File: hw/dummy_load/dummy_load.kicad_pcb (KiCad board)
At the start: 4 copper layers, 100 x 87 mm, 116 parts, among them J1 12V optional, J10 Calib gain, J11 Calib divider, J12 12V in, J2 NTC DUT, J3 NTC Ambient, J4 NTC Heatsink, J5 Fan1, J6 Fan2, J7 NTC Heatsink, J8 NTC Heatsink, J9 NTC Heatsink, Q1 DMN2056U, Q10 DMG2305UX-7, Q2 IRL540NPBF, Q3 IRL540NPBF, Q4 IRL540NPBF, Q5 IRL540NPBF, Q6 IRL540NPBF, Q7 IRL540NPBF, Q8 IRL540NPBF, Q9 IRL540NPBF, U1 LM358, U2 AD620, U21 LM4040B30FTA, U3 LM4040B30FTA, U4 PHOENIX_1017503, U5 74HC4051, U6 AD5272BCP, U7 AD5272BCP, U8 AMS1117-5.0

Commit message: Fix digipot cap value
Signed-off-by: Mateusz Pajak <22417805+Tai-Min@users.noreply.github.com>
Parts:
- C13, C14: value 100n -> 1u
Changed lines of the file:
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@@
 			)
 		)
-		(property "Value" "100n"
+		(property "Value" "1u"
 			(at 0 1.85 90)
 			(layer "F.Fab")
@@
 			)
 		)
-		(property "LCSC Part #" "C24497"
+		(property "LCSC Part #" "C1848"
 			(at 0 0 270)
 			(unlocked yes)
@@
 			)
 		)
-		(property "Value" "100n"
+		(property "Value" "1u"
 			(at 0 1.85 90)
 			(layer "F.Fab")
@@
 			)
 		)
-		(property "LCSC Part #" "C24497"
+		(property "LCSC Part #" "C1848"
 			(at 0 0 90)
 			(unlocked yes)

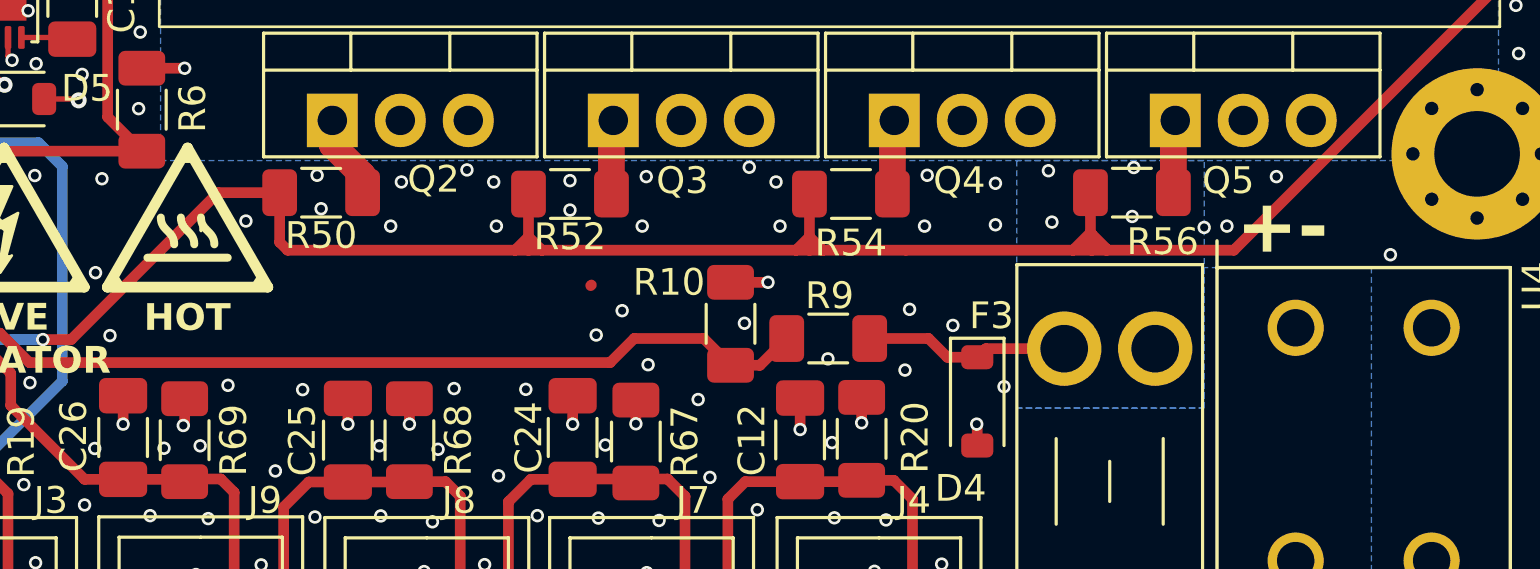
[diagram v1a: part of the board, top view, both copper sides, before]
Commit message: Fix hotspot, remove old schematic file
Signed-off-by: Mateusz Pajak <22417805+Tai-Min@users.noreply.github.com>
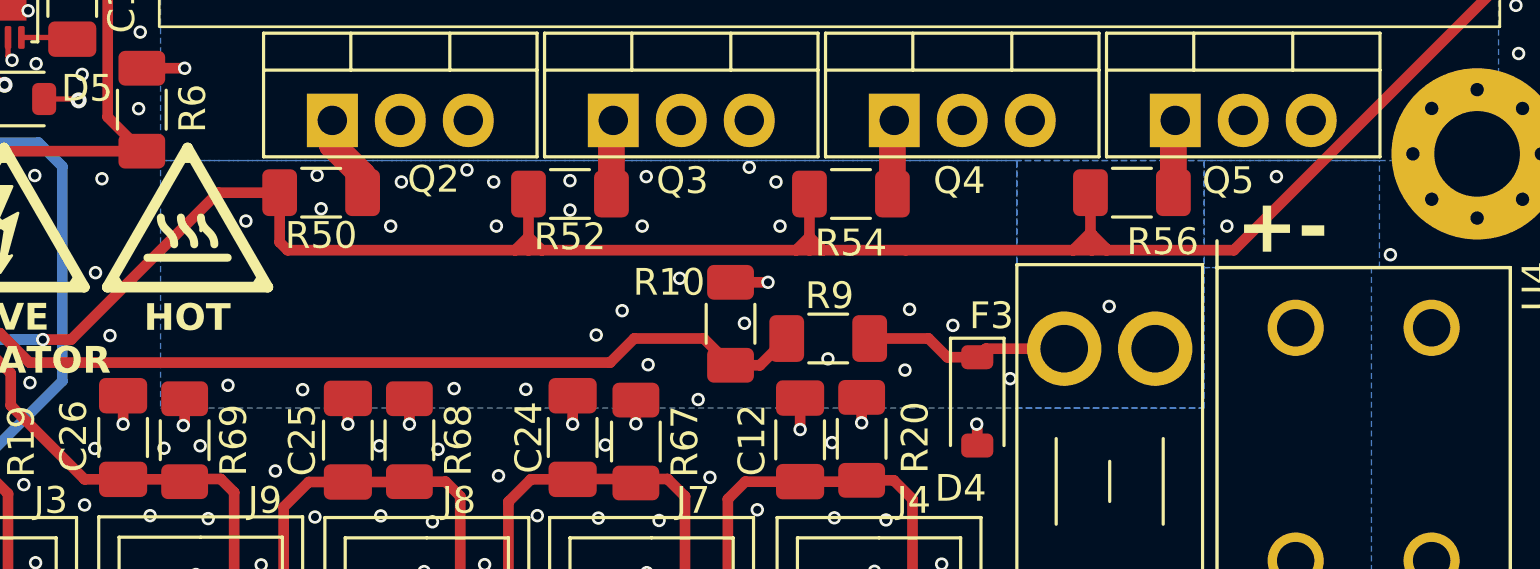
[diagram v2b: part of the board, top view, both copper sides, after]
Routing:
- net GND: vias 465 -> 458
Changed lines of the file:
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@@
 	)
 	(segment
-		(start 163.175 114.225)
-		(end 163.2 114.2)
-		(width 0.4)
-		(layer "F.Cu")
-		(net 4)
-	)
-	(segment
 		(start 123.69375 119.4)
 		(end 124.50625 119.4)
@@
 	)
 	(via
-		(at 180.41 111.85)
-		(size 0.5)
-		(drill 0.3)
-		(layers "F.Cu" "B.Cu")
-		(free yes)
-		(net 4)
-	)
-	(via
 		(at 146.44 99.95)
 		(size 0.5)
@@
 	)
 	(via
-		(at 175.75 110.1)
-		(size 0.5)
-		(drill 0.3)
-		(layers "F.Cu" "B.Cu")
-		(free yes)
-		(net 4)
-	)
-	(via
 		(at 134.91 89.63)
 		(size 0.5)
@@
 	)
 	(via
-		(at 175.65 112)
-		(size 0.5)
-		(drill 0.3)
-		(layers "F.Cu" "B.Cu")
-		(free yes)
-		(net 4)
-	)
-	(via
 		(at 134.75 127.21)
 		(size 0.5)
@@
 	)
 	(via
-		(at 180.28 109.93)
-		(size 0.5)
-		(drill 0.3)
-		(layers "F.Cu" "B.Cu")
-		(free yes)
-		(net 4)
-	)
-	(via
 		(at 133.43 53.81)
 		(size 0.5)
@@
 	)
 	(via
+		(at 182.55 115)
+		(size 0.5)
+		(drill 0.3)
+		(layers "F.Cu" "B.Cu")
+		(free yes)
+		(net 4)
+	)
+	(via
 		(at 150.29 111.81)
 		(size 0.5)
@@
 	)
 	(via
-		(at 186.1 112.05)
-		(size 0.5)
-		(drill 0.3)
-		(layers "F.Cu" "B.Cu")
-		(free yes)
-		(net 4)
-	)
-	(via
 		(at 109.56 61.34)
 		(size 0.5)
@@
 	)
 	(via
-		(at 183.47 109.81)
-		(size 0.5)
-		(drill 0.3)
-		(layers "F.Cu" "B.Cu")
-		(free yes)
-		(net 4)
-	)
-	(via
 		(at 141.85 46.45)
 		(size 0.5)
@@
 	)
 	(via
+		(at 166.5 113.95)
+		(size 0.5)
+		(drill 0.3)
+		(layers "F.Cu" "B.Cu")
+		(free yes)
+		(net 4)
+	)
+	(via
 		(at 137.24 72.46)
 		(size 0.5)
@@
 	)
 	(via
-		(at 178.62 118)
-		(size 0.5)
-		(drill 0.3)
-		(layers "F.Cu" "B.Cu")
-		(free yes)
-		(net 4)
-	)
-	(via
-		(at 178.3 110.4)
+		(at 178.85 117.7)
 		(size 0.5)
 		(drill 0.3)
@@
 	)
 	(via
-		(at 178.3 111.95)
-		(size 0.5)
-		(drill 0.3)
-		(layers "F.Cu" "B.Cu")
-		(free yes)
-		(net 4)
-	)
-	(via
 		(at 110.4 99.1)
 		(size 0.5)
@@
 	)
 	(via
-		(at 183.41 111.64)
-		(size 0.5)
-		(drill 0.3)
-		(layers "F.Cu" "B.Cu")
-		(free yes)
-		(net 4)
-	)
-	(via
 		(at 148.58 120.21)
 		(size 0.5)
@@
 			)
 		)
+	)
+	(zone
+		(net 65)
+		(net_name "/LOAD")
+		(layer "B.Cu")
+		(hatch edge 0.5)
+		(priority 35)
+		(connect_pads
+			(clearance 0.5)
+		)
+		(min_thickness 0.25)
+		(filled_areas_thickness no)
+		(fill yes
+			(thermal_gap 0.5)
+			(thermal_bridge_width 0.5)
+		)
+		(polygon
+			(pts
+				(xy 179.1 109.55) (xy 147.1 109.55) (xy 147.1 118.8) (xy 179.1 118.8)
+			)
+		)
+	)
+	(zone
+		(net 65)
+		(net_name "/LOAD")
+		(layer "B.Cu")
+		(hatch edge 0.5)
+		(priority 34)
+		(connect_pads
+			(clearance 0.5)
+		)
+		(min_thickness 0.25)
+		(filled_areas_thickness no)
+		(fill yes
+			(thermal_gap 0.5)
+			(thermal_bridge_width 0.5)
+		)
+		(polygon
+			(pts
+				(xy 186.1 113.55) (xy 192.65 113.55) (xy 192.65 109.55) (xy 186.1 109.55)
+			)
+		)

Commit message: Replace terminal block, update BOM and datasheets, minor fixes to tracing
Signed-off-by: Mateusz Pajak <22417805+Tai-Min@users.noreply.github.com>
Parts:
- removed U4: PHOENIX_1017503, Library:PHOENIX_1017503
- added X1: WAGO 2604-1102, Library:WAGO-2604-1102, F.Cu at (197.5, 126.2)
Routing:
- net GND: track 67.4 -> 72.3 mm, vias 458 -> 466
- net Net-(Q1-G): track 48.7 -> 52.0 mm

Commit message: Add license on silkscreen
Signed-off-by: Mateusz Pajak <22417805+Tai-Min@users.noreply.github.com>
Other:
- board text added: "Licensed under CERN OHL v.1.2"
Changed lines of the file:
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@@
+		)
+	)
+	(gr_text "Licensed under CERN OHL v.1.2"
+		(at 100.7 75.9 270)
+		(layer "F.SilkS")
+		(effects
+			(font
+				(size 1 1)
+				(thickness 0.2)
+				(bold yes)
+			)
+			(justify bottom)
 		)
 	)
@@
 	)
 	(gr_text "FARELKA REV:${REVISION}"
-		(at 101.78 63.5 270)
+		(at 102.2 63.55 270)
 		(layer "F.SilkS" knockout)
 		(effects
